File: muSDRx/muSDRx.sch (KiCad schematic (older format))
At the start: 89 parts, among them CON1 SJ1-3523N, CON2 SJ1-3523N, J1 Conn_01x02_Male, J11 Conn_01x02_Male, J2 Conn_01x02_Male, J3 Conn_01x02_Male, J4 Conn_01x02_Male, J5 Conn_01x02_Male, J6 Conn_01x02_Male, J9 Conn_01x04_Male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

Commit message: Routed PCB for v0.1.
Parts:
- SW1, SW2: footprint Buttons_Switches_SMD:SW_SPST_B3S-1000 -> Buttons_Switches_THT:SW_PUSH_6mm_h4.3mm
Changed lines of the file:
@@
 encoding utf-8
 Sheet 1 1
-Title "muSDR Receiver"
+Title "muSDRx Receiver"
 Date "2020-07-01"
 Rev "0.1"
@@
 F 0 "SW1" H 1500 7343 50  0000 C CNN
 F 1 "SW_Push" H 1500 7344 50  0001 C CNN
-F 2 "Buttons_Switches_SMD:SW_SPST_B3S-1000" H 1500 7350 50  0001 C CNN
+F 2 "Buttons_Switches_THT:SW_PUSH_6mm_h4.3mm" H 1500 7350 50  0001 C CNN
 F 3 "~" H 1500 7350 50  0001 C CNN
 	1    1500 7150
@@
 F 0 "SW2" H 1500 7250 50  0000 C CNN
 F 1 "SW_Push" H 1500 7544 50  0001 C CNN
-F 2 "Buttons_Switches_SMD:SW_SPST_B3S-1000" H 1500 7550 50  0001 C CNN
+F 2 "Buttons_Switches_THT:SW_PUSH_6mm_h4.3mm" H 1500 7550 50  0001 C CNN
 F 3 "~" H 1500 7550 50  0001 C CNN
 	1    1500 7350
@@
 F 1 "SJ1-3523N" H 8772 4647 60  0001 R CNN
 F 2 "digikey-footprints:Headphone_Jack_2.5mm_SJ1-3523N" H 9300 4900 60  0001 L CNN
-F 3 "https://www.cui.com/product/resource/digikeypdf/sj1-352xn_series.pdf" H 9300 5000 60  0001 L CNN
+F 3 "https://www.cuidevices.com/product/resource/sj1-352xn.pdf" H 9300 5000 60  0001 L CNN
 F 4 "CP1-3523N-ND" H 9300 5100 60  0001 L CNN "Digi-Key_PN"
 F 5 "SJ1-3523N" H 9300 5200 60  0001 L CNN "MPN"
@@
 F 1 "SJ1-3523N" H 8772 1897 60  0001 R CNN
 F 2 "digikey-footprints:Headphone_Jack_2.5mm_SJ1-3523N" H 9300 2150 60  0001 L CNN
-F 3 "https://www.cui.com/product/resource/digikeypdf/sj1-352xn_series.pdf" H 9300 2250 60  0001 L CNN
+F 3 "https://www.cuidevices.com/product/resource/sj1-352xn.pdf" H 9300 2250 60  0001 L CNN
 F 4 "CP1-3523N-ND" H 9300 2350 60  0001 L CNN "Digi-Key_PN"
 F 5 "SJ1-3523N" H 9300 2450 60  0001 L CNN "MPN"

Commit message: Added libraries needed....
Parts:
- J1, J11, J2, J3, J4, J5, J6: symbol Connector:Conn_01x02_Male -> muSDRx-rescue:Conn_01x02_Male-Connector
- J9: symbol Connector:Conn_01x04_Male -> muSDRx-rescue:Conn_01x04_Male-Connector
- P1: symbol lt6231:BNC -> muSDRx-rescue:BNC-lt6231
- Q1: symbol muSDR-rescue:MMBT2222A-TP-dk_Transistors-Bipolar-BJT-Single -> muSDRx-rescue:MMBT2222A-TP-dk_Transistors-Bipolar-BJT-Single-muSDR-rescue
- TP1, TP10, TP11, TP12, TP13, TP14, TP15, TP16, TP17, TP2, TP3, TP4, TP5, TP6, TP7, TP8, TP9: symbol Connector:TestPoint -> muSDRx-rescue:TestPoint-Connector
- U1: symbol LCD1602:LCD1602 -> Display_Character:LCD1602
- U5: symbol lt6231:LT6231 -> muSDRx-rescue:LT6231-lt6231
- Y1: symbol cx3225:CX3225 -> muSDRx-rescue:CX3225-cx3225
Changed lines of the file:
@@
 $EndDescr
 $Comp
-L lt6231:BNC P1
+L muSDRx-rescue:BNC-lt6231 P1
 U 1 1 5EFD1575
 P 3000 1950
@@
 $EndComp
 $Comp
-L Connector:Conn_01x02_Male J3
+L muSDRx-rescue:Conn_01x02_Male-Connector J3
 U 1 1 5EFD7112
 P 2800 2300
@@
 $EndComp
 $Comp
-L lt6231:+4.3V #PWR030
+L muSDRx-rescue:+4.3V-lt6231 #PWR030
 U 1 1 5F00D056
 P 4500 950
@@
 	3000 2400 3000 2500
 $Comp
-L Connector:Conn_01x02_Male J5
+L muSDRx-rescue:Conn_01x02_Male-Connector J5
 U 1 1 5F0DCBF2
 P 3700 7250
@@
 $EndComp
 $Comp
-L muSDR-rescue:MMBT2222A-TP-dk_Transistors-Bipolar-BJT-Single Q1
+L muSDRx-rescue:MMBT2222A-TP-dk_Transistors-Bipolar-BJT-Single-muSDR-rescue Q1
 U 1 1 5F1096CA
 P 1600 2200
@@
 Connection ~ 1700 1700
 $Comp
-L lt6231:+4.3V #PWR014
+L muSDRx-rescue:+4.3V-lt6231 #PWR014
 U 1 1 5F12693B
 P 2100 2850
@@
 Connection ~ 1500 4800
 $Comp
-L LCD1602:LCD1602 U1
+L Display_Character:LCD1602 U1
 U 1 1 5F17AD7C
 P 1500 5900
@@
 AUD_1
 $Comp
-L lt6231:+4.3V #PWR036
+L muSDRx-rescue:+4.3V-lt6231 #PWR036
 U 1 1 5F1AEE46
 P 4950 1450
@@
 	8350 1850 8700 1850
 $Comp
-L Connector:Conn_01x02_Male J11
+L muSDRx-rescue:Conn_01x02_Male-Connector J11
 U 1 1 5F1EC561
 P 8900 2500
@@
 V_IN
 $Comp
-L Connector:TestPoint TP13
+L muSDRx-rescue:TestPoint-Connector TP13
 U 1 1 5F419082
 P 7900 1650
@@
 $EndComp
 $Comp
-L Connector:TestPoint TP14
+L muSDRx-rescue:TestPoint-Connector TP14
 U 1 1 5F419D9A
 P 7900 2400
@@
 	7900 1650 7700 1650
 $Comp
-L Connector:TestPoint TP6
+L muSDRx-rescue:TestPoint-Connector TP6
 U 1 1 5F41BD7E
 P 6200 1550
@@
 Connection ~ 6200 1550
 $Comp
-L Connector:TestPoint TP7
+L muSDRx-rescue:TestPoint-Connector TP7
 U 1 1 5F41CDD2
 P 6350 1750
@@
 Connection ~ 6350 1750
 $Comp
-L Connector:TestPoint TP9
+L muSDRx-rescue:TestPoint-Connector TP9
 U 1 1 5F41D5B8
 P 6500 2300
@@
 $EndComp
 $Comp
-L Connector:TestPoint TP8
+L muSDRx-rescue:TestPoint-Connector TP8
 U 1 1 5F41DC51
 P 6350 2500
@@
 Connection ~ 6500 2300
 $Comp
-L Connector:TestPoint TP5
+L muSDRx-rescue:TestPoint-Connector TP5
 U 1 1 5F420248
 P 3950 1600
@@
 	3950 1950 4150 1950
 $Comp
-L Connector:TestPoint TP2
+L muSDRx-rescue:TestPoint-Connector TP2
 U 1 1 5F5259B2
 P 3550 3300
@@
 $EndComp
 $Comp
-L Connector:TestPoint TP3
+L muSDRx-rescue:TestPoint-Connector TP3
 U 1 1 5F526478
 P 3650 3500
@@
 	3500 3700 3750 3700
 $Comp
-L Connector:TestPoint TP4
+L muSDRx-rescue:TestPoint-Connector TP4
 U 1 1 5F531D25
 P 3750 3700
@@
 	3950 1600 3950 1950
 $Comp
-L Connector:Conn_01x02_Male J4
+L muSDRx-rescue:Conn_01x02_Male-Connector J4
 U 1 1 5F533B86
 P 3400 1750
@@
 J4 for optional BP filter
 $Comp
-L Connector:TestPoint TP1
+L muSDRx-rescue:TestPoint-Connector TP1
 U 1 1 5F549AF1
 P 2100 2850
@@
 	7400 5850 7950 5850
 $Comp
-L Connector:TestPoint TP12
+L muSDRx-rescue:TestPoint-Connector TP12
 U 1 1 5F5BCB4E
 P 7950 5850
@@
 	8150 5150 7400 5150
 $Comp
-L Connector:Conn_01x04_Male J9
+L muSDRx-rescue:Conn_01x04_Male-Connector J9
 U 1 1 5F5F2CED
 P 8650 5450
@@
 $EndComp
 $Comp
-L Connector:TestPoint TP10
+L muSDRx-rescue:TestPoint-Connector TP10
 U 1 1 5F61DDA9
 P 800 3850
@@
 $EndComp
 $Comp
-L Connector:TestPoint TP11
+L muSDRx-rescue:TestPoint-Connector TP11
 U 1 1 5F61EF1D
 P 1100 3850
@@
 	1700 2850 1900 2850
 $Comp
-L lt6231:+4.3V #PWR037
+L muSDRx-rescue:+4.3V-lt6231 #PWR037
 U 1 1 5F8AA93A
 P 4950 5600
@@
 VHI
 $Comp
-L lt6231:+4.3V #PWR053
+L muSDRx-rescue:+4.3V-lt6231 #PWR053
 U 1 1 5F9F0A34
 P 7500 2100
@@
 NoConn ~ 4350 6500
 $Comp
-L Connector:Conn_01x02_Male J2
+L muSDRx-rescue:Conn_01x02_Male-Connector J2
 U 1 1 5FA2C049
 P 850 800
@@
 	2750 7100 2750 7050
 $Comp
-L cx3225:CX3225 Y1
+L muSDRx-rescue:CX3225-cx3225 Y1
 U 1 1 5FAB6A9E
 P 2050 3300
@@
 Drive VHI HIGH to \nset the HIGH logic\nlevel and correct\nDVM for the MCU\nused
 $Comp
-L Connector:TestPoint TP16
+L muSDRx-rescue:TestPoint-Connector TP16
 U 1 1 5FDC5CD5
 P 3950 4600
@@
 $EndComp
 $Comp
-L Connector:TestPoint TP17
+L muSDRx-rescue:TestPoint-Connector TP17
 U 1 1 5FDC80B9
 P 7550 4100
@@
 	7550 4100 7850 4100
 $Comp
-L Connector:TestPoint TP15
+L muSDRx-rescue:TestPoint-Connector TP15
 U 1 1 5FDC962F
 P 1050 5050
@@
 $EndComp
 $Comp
-L lt6231:LT6231 U5
+L muSDRx-rescue:LT6231-lt6231 U5
 U 1 1 5F00833E
 P 7400 1650
@@
 $EndComp
 $Comp
-L lt6231:LT6231 U5
+L muSDRx-rescue:LT6231-lt6231 U5
 U 2 1 5F00967E
 P 7400 2400
@@
 	1150 900  1150 1000
 $Comp
-L Connector:Conn_01x02_Male J1
+L muSDRx-rescue:Conn_01x02_Male-Connector J1
 U 1 1 5F16629C
 P 2100 2250
@@
 Reverse\npolarity\nprotection
 $Comp
-L Connector:Conn_01x02_Male J6
+L muSDRx-rescue:Conn_01x02_Male-Connector J6
 U 1 1 5F23035F
 P 3400 2150

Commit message: Added notes and C11-C15 value changes.
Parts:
- C11, C12, C14, C15: value 0.47uF -> 0.01uF
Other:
- note added: "Insert 1nF for 2 kHz cutoff\nDefault 100 kHz cutoff\n(both op amps) C11 ...C15\nshould be 0.01uF. For 100kHz\nC11..C15 should be 0.47uF\nBW = 1(pi*4*R_ant*C)\nUse 2 kHz for optimum \nMCU demodulation\nand 100 kHz for 96kHz external\ncomputer demodulation."
- note removed: "Insert 1nF for 2 kHz cutoff\nDefault 100 kHz cutoff\n(both op amps)"
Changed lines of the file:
@@
 P 5050 2850
 F 0 "C11" H 5100 2950 50  0000 L CNN
-F 1 "0.47uF" H 5050 2750 50  0000 L CNN
+F 1 "0.01uF" H 5050 2750 50  0000 L CNN
 F 2 "Capacitors_SMD:C_0805" H 5088 2700 50  0001 C CNN
 F 3 "~" H 5050 2850 50  0001 C CNN
@@
 P 5400 2850
 F 0 "C12" H 5450 2950 50  0000 L CNN
-F 1 "0.47uF" H 5400 2750 50  0000 L CNN
+F 1 "0.01uF" H 5400 2750 50  0000 L CNN
 F 2 "Capacitors_SMD:C_0805" H 5438 2700 50  0001 C CNN
 F 3 "~" H 5400 2850 50  0001 C CNN
@@
 P 5750 2850
 F 0 "C14" H 5800 2950 50  0000 L CNN
-F 1 "0.47uF" H 5750 2750 50  0000 L CNN
+F 1 "0.01uF" H 5750 2750 50  0000 L CNN
 F 2 "Capacitors_SMD:C_0805" H 5788 2700 50  0001 C CNN
 F 3 "~" H 5750 2850 50  0001 C CNN
@@
 P 6100 2850
 F 0 "C15" H 6150 2950 50  0000 L CNN
-F 1 "0.47uF" H 6100 2750 50  0000 L CNN
+F 1 "0.01uF" H 6100 2750 50  0000 L CNN
 F 2 "Capacitors_SMD:C_0805" H 6138 2700 50  0001 C CNN
 F 3 "~" H 6100 2850 50  0001 C CNN
@@
 Wire Wire Line
 	1050 2200 950  2200
-Text Notes 7800 950  0    50   ~ 0
-Insert 1nF for 2 kHz cutoff\nDefault 100 kHz cutoff\n(both op amps)
+Text Notes 7800 1300 0    50   ~ 0
+Insert 1nF for 2 kHz cutoff\nDefault 100 kHz cutoff\n(both op amps)  C11 ...C15\nshould be 0.01uF.  For 100kHz\nC11..C15 should be 0.47uF\nBW = 1(pi*4*R_ant*C)\nUse 2 kHz for optimum \nMCU demodulation\nand 100 kHz for 96kHz external\ncomputer demodulation.
 $Comp
 L Device:C C18

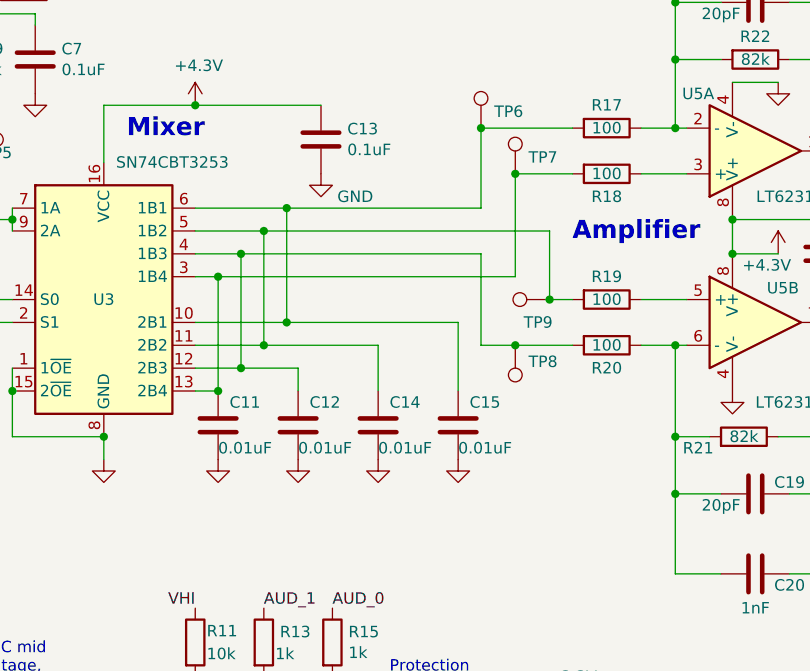
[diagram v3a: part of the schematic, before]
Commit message: Changed R18 and R19 to 0 Ohms for better noise performance at the sacrifice of a little DC offset from input bias currents
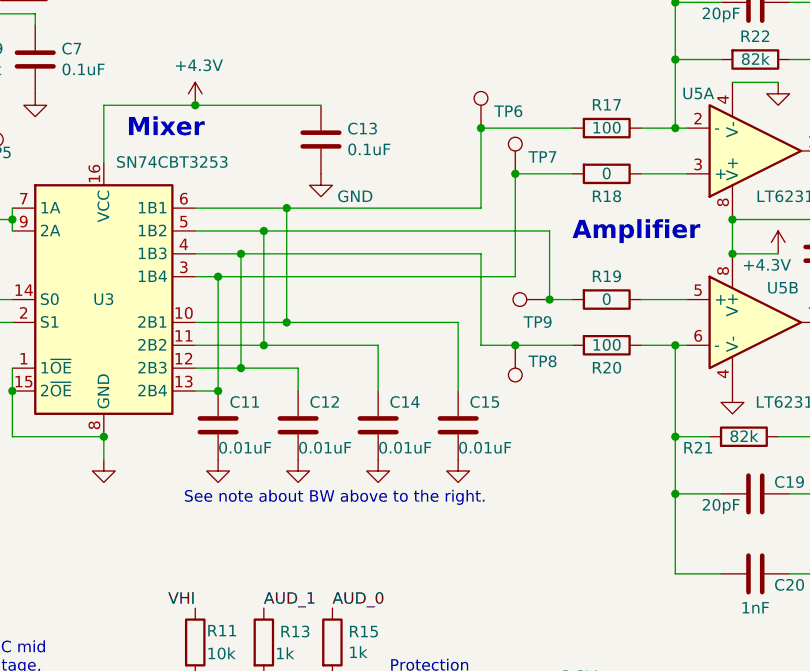
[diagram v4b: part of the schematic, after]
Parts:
- R18, R19: value 100 -> 0
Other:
- note added: "See note about BW above to the right."
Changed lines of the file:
@@
 P 6750 1750
 F 0 "R18" V 6850 1750 50  0000 C CNN
-F 1 "100" V 6750 1750 50  0000 C CNN
+F 1 "0" V 6750 1750 50  0000 C CNN
 F 2 "Resistors_SMD:R_0805" V 6680 1750 50  0001 C CNN
 F 3 "~" H 6750 1750 50  0001 C CNN
@@
 P 6750 2300
 F 0 "R19" V 6650 2300 50  0000 C CNN
-F 1 "100" V 6750 2300 50  0000 C CNN
+F 1 "0" V 6750 2300 50  0000 C CNN
 F 2 "Resistors_SMD:R_0805" V 6680 2300 50  0001 C CNN
 F 3 "~" H 6750 2300 50  0001 C CNN
@@
 	-1   0    0    -1
 $EndComp
+Text Notes 4900 3200 0    50   ~ 0
+See note about BW above to the right.
 $EndSCHEMATC
